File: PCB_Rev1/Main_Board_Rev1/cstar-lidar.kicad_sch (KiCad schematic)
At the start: 0 parts

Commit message: LDO component files imported
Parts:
- added J3: 532610771, CSTAR-MainBoard-Footprints:MOLEX_532610771, symbol 532610771:532610771
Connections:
- new net +5V: J3.1, J3.5
- new net GND: J3.3, J3.4, J3.S1 (SHIELD1), J3.S2 (SHIELD2)
- new net GPIO14: J3.6
- new net GPIO15: J3.7
- new net GPIO17: J3.2
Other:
- note added: "Lidar Connector"

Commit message: Update cstar-lidar.kicad_sch
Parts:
- J3: footprint CSTAR-MainBoard-Footprints:MOLEX_532610771 -> Connector_Molex:Molex_PicoBlade_53261-0771_1x07-1MP_P1.25mm_Horizontal
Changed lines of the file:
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@@
 			)
 		)
-		(property "Footprint" "CSTAR-MainBoard-Footprints:MOLEX_532610771"
+		(property "Footprint" "Connector_Molex:Molex_PicoBlade_53261-0771_1x07-1MP_P1.25mm_Horizontal"
 			(at 172.72 95.25 0)
 			(effects

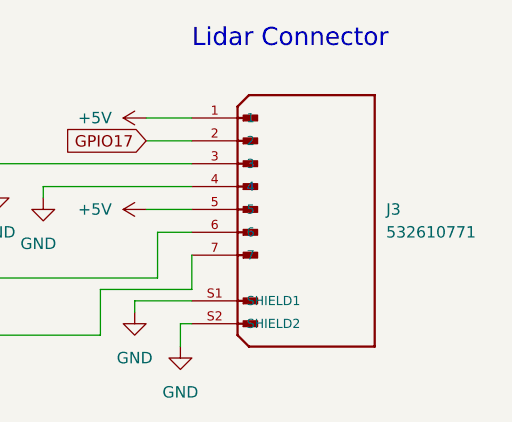
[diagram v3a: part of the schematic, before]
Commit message: Audio Subsystem Re-created
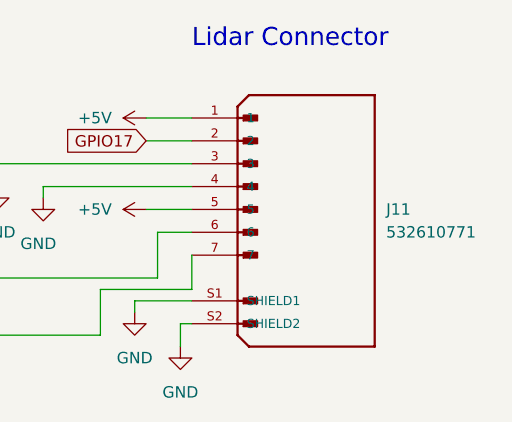
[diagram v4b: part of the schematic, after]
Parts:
- renumbered J3 to J11
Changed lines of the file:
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@@
 		(dnp no)
 		(fields_autoplaced yes)
-		(property "Reference" "#PWR05"
+		(property "Reference" "#PWR0102"
 			(at 158.75 95.25 0)
 			(effects
@@
 		)
 		(instances
-			(project "cstar-lidar"
-				(path "/7fb126c7-7496-463a-9dd5-726b856075e6"
-					(reference "#PWR05")
-					(unit 1)
-				)
-			)
 			(project "Main_Board_Rev1"
 				(path "/8f5a23de-a1fa-4202-92fb-c2ac3de0338c/4da50182-4bfb-4740-9f93-3f86bef2b2e8"
 					(reference "#PWR0102")
+					(unit 1)
+				)
+				(path "/8f5a23de-a1fa-4202-92fb-c2ac3de0338c/ddfb4fd8-d336-4db3-9d74-da06ae92f0f2"
+					(reference "#PWR051")
 					(unit 1)
 				)
@@
 		(dnp no)
 		(fields_autoplaced yes)
-		(property "Reference" "#PWR03"
+		(property "Reference" "#PWR0103"
 			(at 153.67 113.03 0)
 			(effects
@@
 		)
 		(instances
-			(project "cstar-lidar"
-				(path "/7fb126c7-7496-463a-9dd5-726b856075e6"
-					(reference "#PWR03")
-					(unit 1)
-				)
-			)
 			(project "Main_Board_Rev1"
 				(path "/8f5a23de-a1fa-4202-92fb-c2ac3de0338c/4da50182-4bfb-4740-9f93-3f86bef2b2e8"
 					(reference "#PWR0103")
+					(unit 1)
+				)
+				(path "/8f5a23de-a1fa-4202-92fb-c2ac3de0338c/ddfb4fd8-d336-4db3-9d74-da06ae92f0f2"
+					(reference "#PWR049")
 					(unit 1)
 				)
@@
 		(dnp no)
 		(fields_autoplaced yes)
-		(property "Reference" "#PWR06"
+		(property "Reference" "#PWR0104"
 			(at 158.75 116.84 0)
 			(effects
@@
 		)
 		(instances
-			(project "cstar-lidar"
-				(path "/7fb126c7-7496-463a-9dd5-726b856075e6"
-					(reference "#PWR06")
-					(unit 1)
-				)
-			)
 			(project "Main_Board_Rev1"
 				(path "/8f5a23de-a1fa-4202-92fb-c2ac3de0338c/4da50182-4bfb-4740-9f93-3f86bef2b2e8"
 					(reference "#PWR0104")
+					(unit 1)
+				)
+				(path "/8f5a23de-a1fa-4202-92fb-c2ac3de0338c/ddfb4fd8-d336-4db3-9d74-da06ae92f0f2"
+					(reference "#PWR052")
 					(unit 1)
 				)
@@
 		(dnp no)
 		(fields_autoplaced yes)
-		(property "Reference" "#PWR04"
+		(property "Reference" "#PWR0101"
 			(at 158.75 85.09 0)
 			(effects
@@
 		)
 		(instances
-			(project "cstar-lidar"
-				(path "/7fb126c7-7496-463a-9dd5-726b856075e6"
-					(reference "#PWR04")
-					(unit 1)
-				)
-			)
 			(project "Main_Board_Rev1"
 				(path "/8f5a23de-a1fa-4202-92fb-c2ac3de0338c/4da50182-4bfb-4740-9f93-3f86bef2b2e8"
 					(reference "#PWR0101")
+					(unit 1)
+				)
+				(path "/8f5a23de-a1fa-4202-92fb-c2ac3de0338c/ddfb4fd8-d336-4db3-9d74-da06ae92f0f2"
+					(reference "#PWR050")
 					(unit 1)
 				)
@@
 		(on_board yes)
 		(dnp no)
-		(property "Reference" "#PWR02"
+		(property "Reference" "#PWR0105"
 			(at 143.51 100.33 0)
 			(effects
@@
 		)
 		(instances
-			(project "cstar-lidar"
-				(path "/7fb126c7-7496-463a-9dd5-726b856075e6"
-					(reference "#PWR02")
-					(unit 1)
-				)
-			)
 			(project "Main_Board_Rev1"
 				(path "/8f5a23de-a1fa-4202-92fb-c2ac3de0338c/4da50182-4bfb-4740-9f93-3f86bef2b2e8"
 					(reference "#PWR0105")
+					(unit 1)
+				)
+				(path "/8f5a23de-a1fa-4202-92fb-c2ac3de0338c/ddfb4fd8-d336-4db3-9d74-da06ae92f0f2"
+					(reference "#PWR048")
 					(unit 1)
 				)
@@
 		(dnp no)
 		(fields_autoplaced yes)
-		(property "Reference" "J3"
+		(property "Reference" "J11"
 			(at 181.61 95.25 0)
 			(effects
@@
 		)
 		(instances
-			(project "cstar-lidar"
-				(path "/7fb126c7-7496-463a-9dd5-726b856075e6"
-					(reference "J3")
-					(unit 1)
-				)
-			)
 			(project "Main_Board_Rev1"
 				(path "/8f5a23de-a1fa-4202-92fb-c2ac3de0338c/4da50182-4bfb-4740-9f93-3f86bef2b2e8"
 					(reference "J11")
+					(unit 1)
+				)
+				(path "/8f5a23de-a1fa-4202-92fb-c2ac3de0338c/ddfb4fd8-d336-4db3-9d74-da06ae92f0f2"
+					(reference "J12")
 					(unit 1)
 				)
@@
 		(dnp no)
 		(fields_autoplaced yes)
-		(property "Reference" "#PWR01"
+		(property "Reference" "#PWR0106"
 			(at 138.43 99.06 0)
 			(effects
@@
 		)
 		(instances
-			(project "cstar-lidar"
-				(path "/7fb126c7-7496-463a-9dd5-726b856075e6"
-					(reference "#PWR01")
-					(unit 1)
-				)
-			)
 			(project "Main_Board_Rev1"
 				(path "/8f5a23de-a1fa-4202-92fb-c2ac3de0338c/4da50182-4bfb-4740-9f93-3f86bef2b2e8"
@@
 					(unit 1)
 				)
+				(path "/8f5a23de-a1fa-4202-92fb-c2ac3de0338c/ddfb4fd8-d336-4db3-9d74-da06ae92f0f2"
+					(reference "#PWR045")
+					(unit 1)
+				)

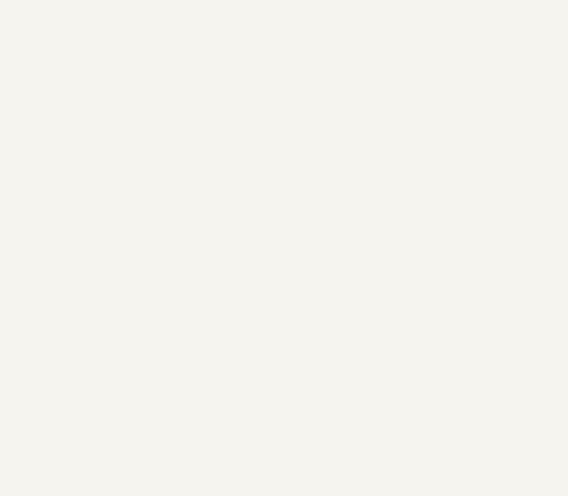
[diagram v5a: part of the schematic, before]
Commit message: Power nets updated in all schematics
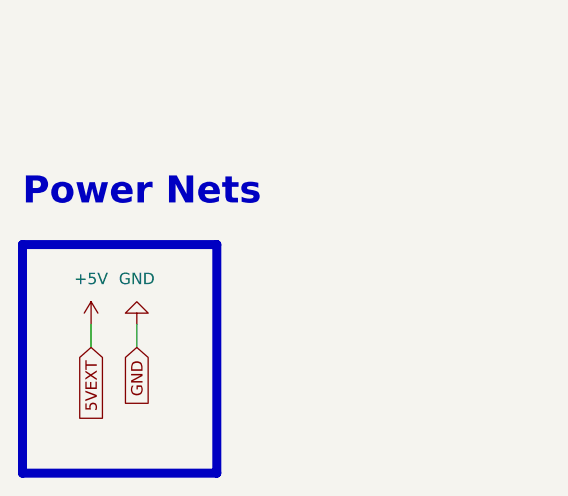
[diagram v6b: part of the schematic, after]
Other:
- note added: "Power Nets"
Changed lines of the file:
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@@
+	(wire
+		(pts
+			(xy 53.34 143.51) (xy 53.34 146.05)
+		)
+		(stroke
+			(width 0)
+			(type default)
+		)
+	)
 	(wire
 		(pts
@@
 			(width 0)
 			(type default)
+		)
+	)
+	(wire
+		(pts
+			(xy 58.42 143.51) (xy 58.42 146.05)
+		)
+		(stroke
+			(width 0)
+			(type default)
+		)
+	)
+	(rectangle
+		(start 45.72 134.62)
+		(end 67.31 160.02)
+		(stroke
+			(width 1)
+			(type default)
+		)
+		(fill
+			(type none)
 		)
 	)
@@
 		)
 	)
+	(text "Power Nets"
+		(exclude_from_sim no)
+		(at 45.72 130.556 0)
+		(effects
+			(font
+				(size 3 3)
+				(thickness 0.6)
+				(bold yes)
+			)
+			(justify left bottom)
+		)
+	)
+	(global_label "GND"
+		(shape input)
+		(at 58.42 146.05 270)
+		(fields_autoplaced yes)
+		(effects
+			(font
+				(size 1.27 1.27)
+			)
+			(justify right)
+		)
+		(property "Intersheetrefs" "${INTERSHEET_REFS}"
+			(at 58.42 152.9057 90)
+			(effects
+				(font
+					(size 1.27 1.27)
+				)
+				(justify right)
+				(hide yes)
+			)
+		)
+	)
 	(global_label "GPIO15"
 		(shape input)
@@
 		(property "Intersheetrefs" "${INTERSHEET_REFS}"
 			(at 108.2305 109.22 0)
+			(effects
+				(font
+					(size 1.27 1.27)
+				)
+				(justify right)
+				(hide yes)
+			)
+		)
+	)
+	(global_label "5VEXT"
+		(shape input)
+		(at 53.34 146.05 270)
+		(fields_autoplaced yes)
+		(effects
+			(font
+				(size 1.27 1.27)
+			)
+			(justify right)
+		)
+		(property "Intersheetrefs" "${INTERSHEET_REFS}"
+			(at 53.34 154.6594 90)
 			(effects
 				(font
@@
 	)
 	(symbol
+		(lib_id "power:+5V")
+		(at 53.34 143.51 0)
+		(unit 1)
+		(exclude_from_sim no)
+		(in_bom yes)
+		(on_board yes)
+		(dnp no)
+		(fields_autoplaced yes)
+		(property "Reference" "#PWR060"
+			(at 53.34 147.32 0)
+			(effects
+				(font
+					(size 1.27 1.27)
+				)
+				(hide yes)
+			)
+		)
+		(property "Value" "+5V"
+			(at 53.34 138.43 0)
+			(effects
+				(font
+					(size 1.27 1.27)
+				)
+			)
+		)
+		(property "Footprint" ""
+			(at 53.34 143.51 0)
+			(effects
+				(font
+					(size 1.27 1.27)
+				)
+				(hide yes)
+			)
+		)
+		(property "Datasheet" ""
+			(at 53.34 143.51 0)
+			(effects
+				(font
+					(size 1.27 1.27)
+				)
+				(hide yes)
+			)
+		)
+		(property "Description" "Power symbol creates a global label with name \"+5V\""
+			(at 53.34 143.51 0)
+			(effects
+				(font
+					(size 1.27 1.27)
+				)
+				(hide yes)
+			)
+		)
+		(pin "1"
+		)
+		(instances
+			(project "Main_Board_Rev1"
+				(path "/8f5a23de-a1fa-4202-92fb-c2ac3de0338c/4da50182-4bfb-4740-9f93-3f86bef2b2e8"
+					(reference "#PWR060")
+					(unit 1)
+				)
+			)
+		)
+	)
+	(symbol
 		(lib_id "power:GND")
 		(at 153.67 106.68 0)
@@
 					(unit 1)
 				)
+			)
+		)
+	)
+	(symbol
+		(lib_id "power:GND")
+		(at 58.42 143.51 180)
+		(unit 1)
+		(exclude_from_sim no)
+		(in_bom yes)
+		(on_board yes)
+		(dnp no)
+		(fields_autoplaced yes)
+		(property "Reference" "#PWR065"
+			(at 58.42 137.16 0)
+			(effects
+				(font
+					(size 1.27 1.27)
+				)
+				(hide yes)
+			)
+		)
+		(property "Value" "GND"
+			(at 58.42 138.43 0)
+			(effects
+				(font
+					(size 1.27 1.27)
+				)
+			)
+		)
+		(property "Footprint" ""
+			(at 58.42 143.51 0)
+			(effects
+				(font
+					(size 1.27 1.27)
+				)
+				(hide yes)
+			)
+		)
+		(property "Datasheet" ""
+			(at 58.42 143.51 0)
+			(effects
+				(font
+					(size 1.27 1.27)
+				)
+				(hide yes)
+			)
+		)
+		(property "Description" "Power symbol creates a global label with name \"GND\" , ground"
+			(at 58.42 143.51 0)
+			(effects
+				(font
+					(size 1.27 1.27)
+				)
+				(hide yes)
+			)
+		)
+		(pin "1"
+		)
+		(instances
+			(project "Main_Board_Rev1"
+				(path "/8f5a23de-a1fa-4202-92fb-c2ac3de0338c/4da50182-4bfb-4740-9f93-3f86bef2b2e8"
+					(reference "#PWR065")
+					(unit 1)
+				)

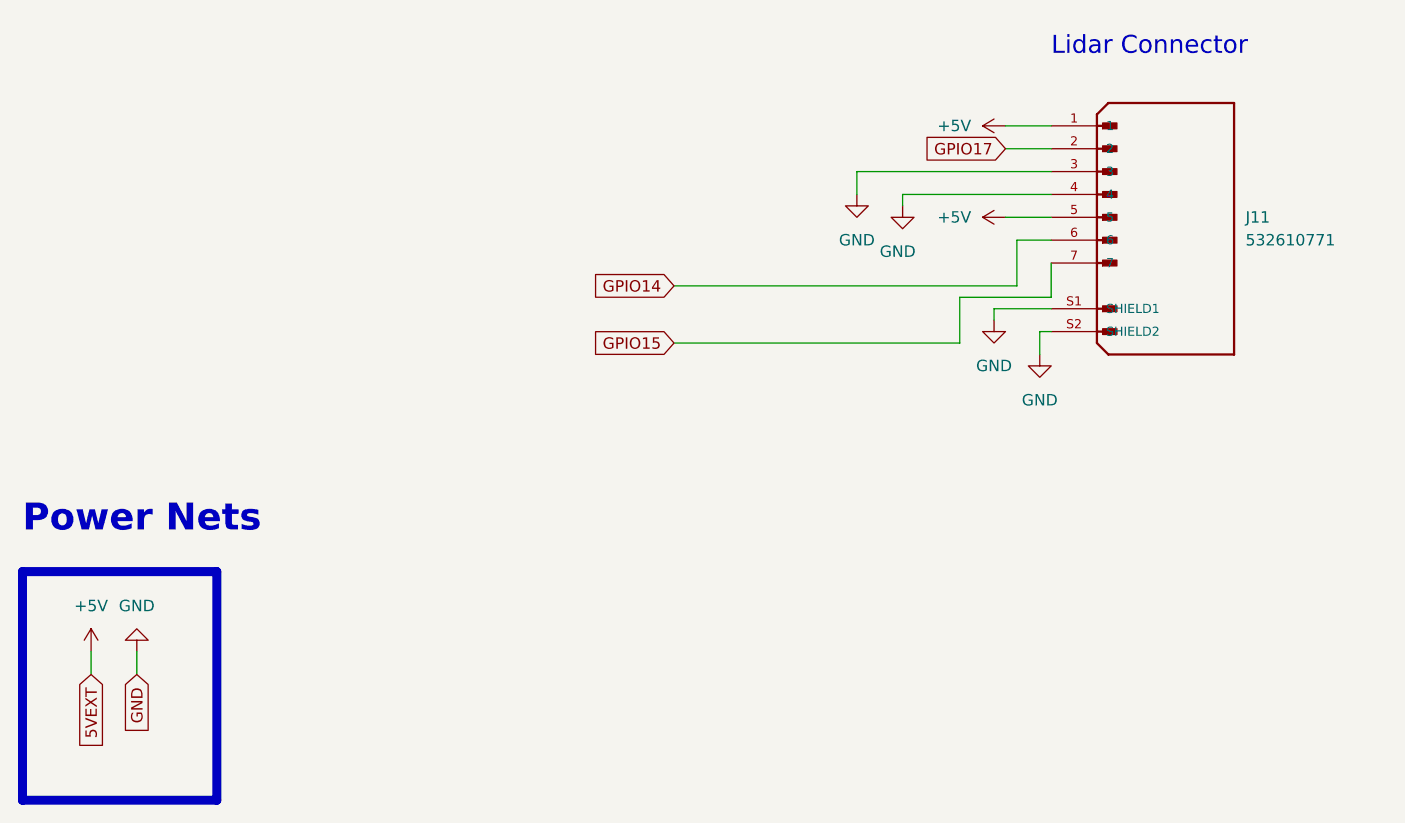
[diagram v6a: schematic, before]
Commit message: Connections to RPi GPIO Pins + Eliminating Errors from Layout
Global net connections made from RPi GPIO pins.
Error for mounting hole corrected -> mounting hole symbol imported into schematic and correct footprint assigned.
Warnings for J10, J11, J12 connectors resolved- imported footprint for the connector from online (error in the one imported from KiCAD libraries with pins S1 and S2 labeled as MP in the footprint)
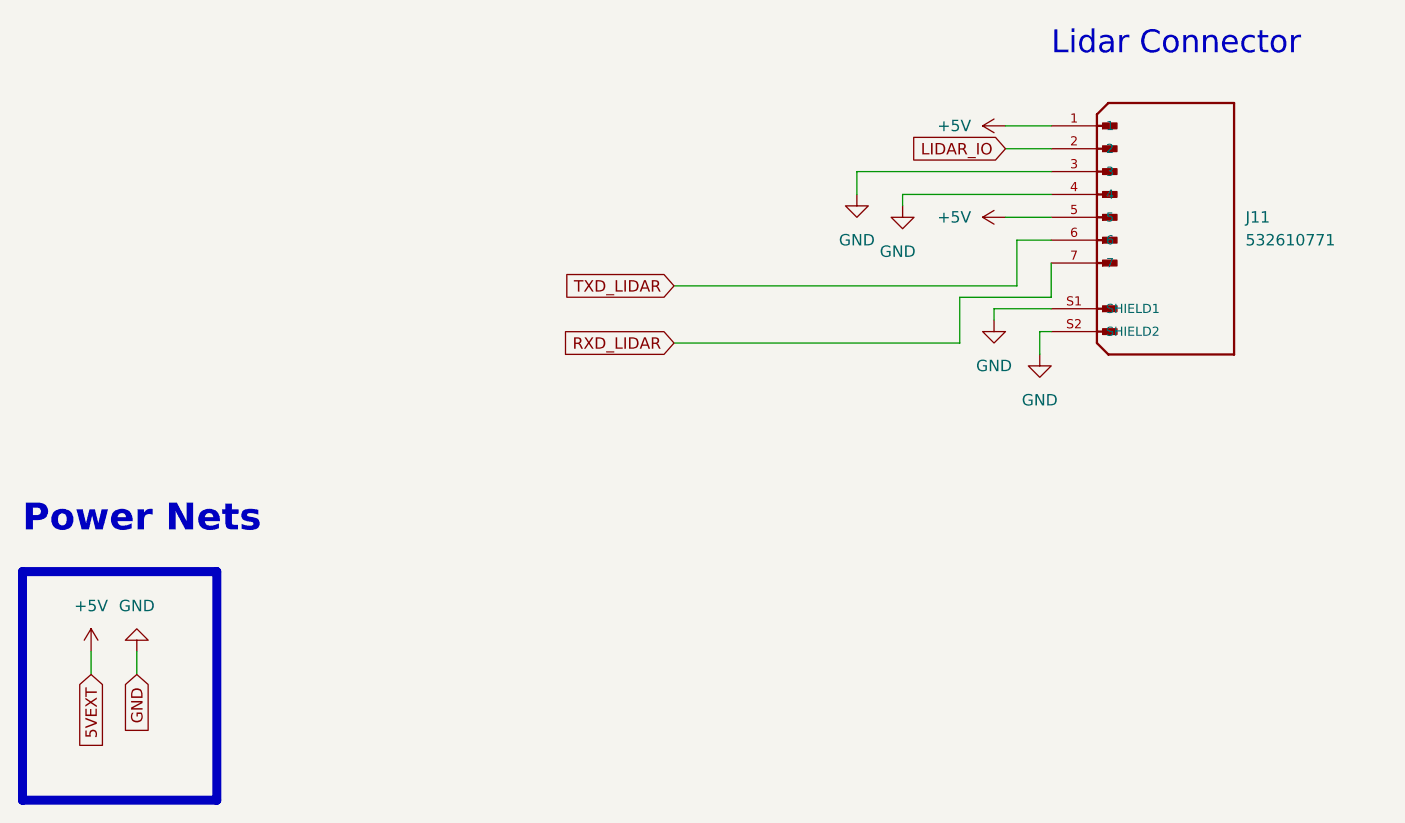
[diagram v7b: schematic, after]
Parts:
- J11: footprint Connector_Molex:Molex_PicoBlade_53261-0771_1x07-1MP_P1.25mm_Horizontal -> Footprints:MOLEX_connector
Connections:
- net GPIO14 renamed TXD_LIDAR
- net GPIO15 renamed RXD_LIDAR
- net GPIO17 renamed LIDAR_IO
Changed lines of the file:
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@@
 		(effects
 			(font
-				(size 2 2)
+				(size 2.54 2.54)
+				(thickness 0.25)
 			)
 			(justify left bottom)
@@
 		)
 	)
-	(global_label "GPIO15"
+	(global_label "RXD_LIDAR"
 		(shape input)
 		(at 118.11 109.22 180)
@@
 		)
 		(property "Intersheetrefs" "${INTERSHEET_REFS}"
-			(at 108.2305 109.22 0)
+			(at 105.1462 109.22 0)
 			(effects
 				(font
@@
 		)
 	)
-	(global_label "GPIO14"
+	(global_label "TXD_LIDAR"
 		(shape input)
 		(at 118.11 102.87 180)
@@
 		)
 		(property "Intersheetrefs" "${INTERSHEET_REFS}"
-			(at 108.2305 102.87 0)
+			(at 105.4486 102.87 0)
 			(effects
 				(font
@@
 		)
 	)
-	(global_label "GPIO17"
+	(global_label "LIDAR_IO"
 		(shape input)
 		(at 154.94 87.63 180)
@@
 		)
 		(property "Intersheetrefs" "${INTERSHEET_REFS}"
-			(at 145.0605 87.63 0)
+			(at 143.7904 87.63 0)
 			(effects
 				(font
@@
 			)
 		)
-		(property "Footprint" "Connector_Molex:Molex_PicoBlade_53261-0771_1x07-1MP_P1.25mm_Horizontal"
+		(property "Footprint" "Footprints:MOLEX_connector"
 			(at 172.72 95.25 0)
 			(effects
